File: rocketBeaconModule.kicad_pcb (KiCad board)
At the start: 2 copper layers, 57.2 x 57.2 mm, 96 parts, among them J1 TYPE-C-31-M-12, J2 PWR, J3 GND, J4 PWR, J5 GND, J6 Conn_01x03_Pin, P1 AntMount, U1 STM32F401CCU6, U2 CP2102N-Axx-xQFN20, U3 CC1200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

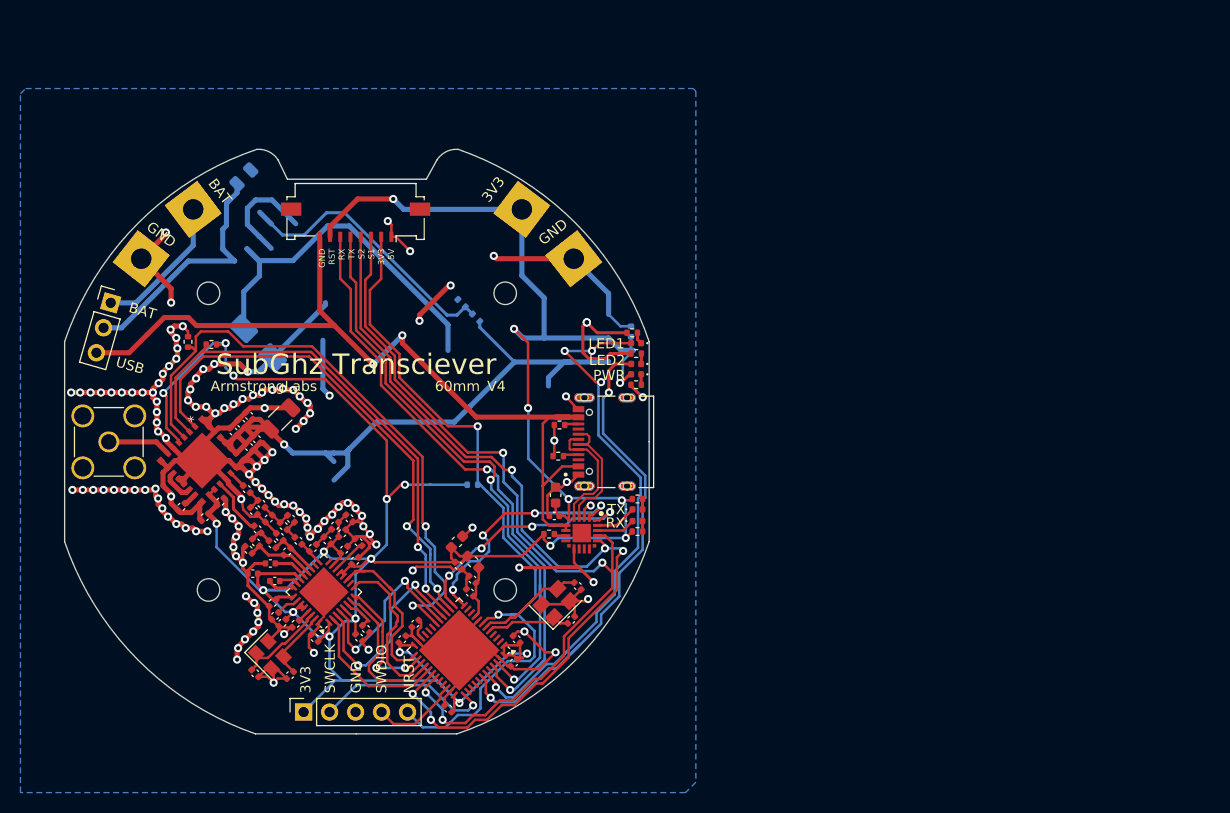
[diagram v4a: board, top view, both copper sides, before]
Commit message: added Mitsibushi Amp w/ supporting gate control circuitry, switching, and temperature monitoring
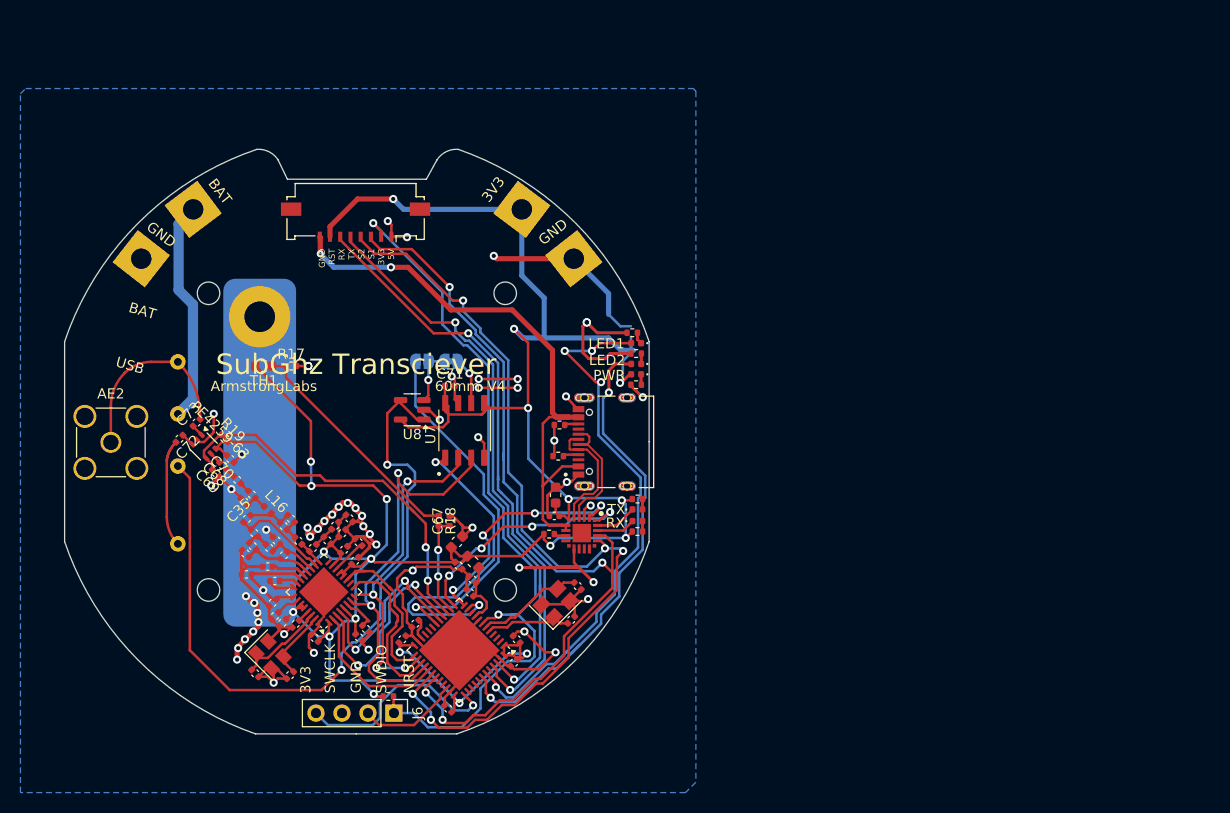
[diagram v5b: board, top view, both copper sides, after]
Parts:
- removed C14, C42: 10nF, Capacitor_SMD:C_0402_1005Metric
- removed C38, C39: 220pF, Capacitor_SMD:C_0402_1005Metric
- removed C40: 1uF, Capacitor_SMD:C_0402_1005Metric
- removed C41: 1nF, Capacitor_SMD:C_0402_1005Metric
- removed C43: 220uF, Capacitor_SMD:C_1206_3216Metric
- removed C44: 10uF, Capacitor_SMD:C_0402_1005Metric
- removed C45: 100uF, Capacitor_SMD:C_0805_2012Metric
- removed D6: SS34, Diode_SMD:D_SMA
- removed P1: AntMount, Connector_Coaxial:SMA_Amphenol_132134-11_Vertical
- removed R14, R15: 1k, Resistor_SMD:R_0402_1005Metric
- removed R16: 1.8k, Resistor_SMD:R_0402_1005Metric
- removed R2: 0, Capacitor_SMD:C_0402_1005Metric
- removed SWD1: FLASH, Connector_PinSocket_2.54mm:PinSocket_1x05_P2.54mm_Vertical
- removed U4: SKY65366-21, SKY65366:SKY65366-21_SKY
- added AE2: Antenna_Shield, Connector_Coaxial:SMA_Amphenol_132134-11_Vertical, F.Cu at (48.0, 126.8)
- added C67: 0.1uF, Capacitor_SMD:C_0402_1005Metric, F.Cu at (81.1, 134.5)
- added C68: 100pF, Capacitor_SMD:C_0402_1005Metric, F.Cu at (58.9, 129.1)
- added C69: 10nF, Capacitor_SMD:C_0402_1005Metric, F.Cu at (58.2, 129.8)
- added C70: 0.1uF, Capacitor_SMD:C_0402_1005Metric, F.Cu at (59.6, 128.4)
- added C71: 0.1uF, Capacitor_SMD:C_0402_1005Metric, F.Cu at (81.1, 121.3)
- added C72: 100pF, Capacitor_SMD:C_0402_1005Metric, F.Cu at (54.7, 126.4)
- added C73: 100pF, Capacitor_SMD:C_0402_1005Metric, F.Cu at (56.3, 124.9)
- added JP3: SolderJumper_2_Bridged, Jumper:SolderJumper-2_P1.3mm_Bridged_RoundedPad1.0x1.5mm, B.Cu at (81.2, 118.9)
- added JP4: SolderJumper_2_Open, Jumper:SolderJumper-2_P1.3mm_Open_RoundedPad1.0x1.5mm, B.Cu at (78.4, 118.9)
- added L16: 43nH, Inductor_SMD:L_0402_1005Metric, F.Cu at (63.3, 133.4)
- added PE4259-63: 4259-63, Package_TO_SOT_SMD:SOT-363_SC-70-6, F.Cu at (57.0, 127.2)
- added R19: 1k, Resistor_SMD:R_0402_1005Metric, F.Cu at (59.1, 126.4)
- added RFAMP2: RA07H4047M-101, RA07H4047m:RA07h4047M, B.Cu at (62.5, 127.8)
- added TH1: PT100, Resistor_SMD:R_0603_1608Metric, F.Cu at (62.9, 119.3)
- added U7: MCP41010, MCP41010:SOIC127P599X175-8N, F.Cu at (82.5, 125.6)
- added U8: MCP6001-OT, Package_TO_SOT_SMD:SOT-23-5, F.Cu at (77.4, 123.6)
- J6: value Conn_01x03_Pin -> Conn_01x04_Pin; footprint Connector_PinHeader_2.54mm:PinHeader_1x03_P2.54mm_Vertical -> Connector_PinHeader_2.54mm:PinHeader_1x04_P2.54mm_Vertical
- R1: moved to F.Cu
- R17: value 3.9k -> 100; moved to F.Cu
- R18: value 1k -> 1000; moved to F.Cu
- R9: value 18k -> 18
- moved J6 48.7 mm to (75.6, 153.3), turned to -90 degrees
- moved R18 26.4 mm to (80.0, 134.5), turned to -90 degrees
- moved R1 22.3 mm to (75.1, 151.6)
- moved R17 18.7 mm to (65.6, 119.3), turned to 0 degrees
- moved C35 2.13 mm to (61.3, 134.3), turned to 45 degrees
- moved C37 1.31 mm to (61.0, 132.6), turned to 135 degrees
- moved L7 1.31 mm to (61.7, 131.9)
- moved R13 1.31 mm to (60.3, 130.5)
- moved C24 0.63 mm to (61.2, 139.7)
- moved C32 0.48 mm to (61.1, 137.7)
- moved C33 0.48 mm to (63.4, 137.1)
- moved L2 0.48 mm to (64.9, 137.8)
- moved L4 0.48 mm to (64.2, 136.4)
- moved L6 0.48 mm to (62.0, 135.7)
- moved L3 0.48 mm to (61.8, 136.9)
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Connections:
- net SPI2_SCK renamed DPOT_SCLK
- net SPI_MOSI renamed DPOT_MOSI
- C1 pad 1: FEM_VPC -> +3.3V
- C12 pad 1: FEM_VPC -> +3.3V
- C13 pad 1: FEM_VPC -> +3.3V
- C15 pad 1: FEM_VPC -> +3.3V
- C17 pad 1: FEM_VPC -> +3.3V
- C18 pad 1: FEM_VPC -> +3.3V
- C19 pad 1: FEM_VPC -> +3.3V
- C2 pad 1: FEM_VPC -> +3.3V
- C22 pad 1: FEM_VPC -> +3.3V
- C24 pad 1: FEM_VPC -> +3.3V
- C26 pad 2: FEM_VPC -> +3.3V
- C27 pad 1: FEM_VPC -> +3.3V
- C28 pad 2: FEM_VPC -> +3.3V
- C29 pad 2: FEM_VPC -> +3.3V
- C35 pad 1: Net-(C34-Pad1) -> Net-(U3-TRX_SW)
- C35 pad 2: GND -> Net-(C34-Pad1)
- C4 pad 1: FEM_VPC -> +3.3V
- C5 pad 1: FEM_VPC -> +3.3V
- C7 pad 1: FEM_VPC -> +3.3V
- C8 pad 1: FEM_VPC -> +3.3V
- D1 pad 2: FEM_VPC -> +3.3V
- EX1 pad 7: FEM_VPC -> +3.3V
- FB1 pad 2: FEM_VPC -> +3.3V
- J2 pad 1: FEM_VPC -> +3.3V
- J6 pad 1: +BATT -> /NRST
- J6 pad 2: /HV_SUPPLY -> /SWDIO
- J6 pad 3: VBUS -> GND
- L6 pad 2: Net-(U4-RX0) -> Net-(U3-TRX_SW)
- L7 pad 1: Net-(C34-Pad1) -> Net-(C37-Pad1)
- L7 pad 2: Net-(C37-Pad1) -> Net-(L7-Pad2)
- R1 pad 2: FEM_VPC -> +3.3V
- R10 pad 1: FEM_VPC -> +3.3V
- R11 pad 1: FEM_VPC -> +3.3V
- R12 pad 1: FEM_VPC -> +3.3V
- R13 pad 1: Net-(C37-Pad1) -> Net-(L7-Pad2)
- R17 pad 1: Net-(U5-FB) -> Net-(R17-Pad1)
- R17 pad 2: +3V9 -> GND
- R18 pad 1: FEM_VPC -> Net-(R17-Pad1)
- R18 pad 2: GND -> TEMPSENSORADC
- R9 pad 2: FEM_VPC -> +3.3V
- U1 pad 1: FEM_VPC -> +3.3V
- U1 pad 11: unconnected-(U1-PA1-Pad11) -> DPOT_CS
- U1 pad 14: FEM_TR -> TEMPSENSORADC
- U1 pad 15: FEM_EN -> AMP_SW_CTRL
- U1 pad 18: FEM_BYP -> AMP_ON
- U1 pad 24: FEM_VPC -> +3.3V
- U1 pad 36: FEM_VPC -> +3.3V
- U1 pad 48: FEM_VPC -> +3.3V
- U2 pad 6: FEM_VPC -> +3.3V
- U3 pad 1: FEM_VPC -> +3.3V
- U3 pad 12: FEM_VPC -> +3.3V
- U3 pad 13: FEM_VPC -> +3.3V
- U3 pad 15: FEM_VPC -> +3.3V
- U3 pad 18: unconnected-(U3-TRX_SW-Pad18) -> Net-(U3-TRX_SW)
- U3 pad 22: FEM_VPC -> +3.3V
- U3 pad 25: FEM_VPC -> +3.3V
- U3 pad 27: FEM_VPC -> +3.3V
- U3 pad 28: FEM_VPC -> +3.3V
- U3 pad 5: FEM_VPC -> +3.3V
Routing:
- net FEM_VPC: track 301.6 -> 0.00 mm, vias 23 -> 0
- net +3.3V: track 0.00 -> 291.5 mm, vias 0 -> 21
- net GND: track 362.0 -> 210.1 mm, vias 128 -> 55
- net Net-(RFAMP2-GATE_VOLTAGE_(VGG)): track 0.00 -> 71.4 mm, vias 0 -> 2
- net +3V9: track 70.7 -> 0.00 mm, vias 1 -> 0
- net FEM_BYP: track 60.6 -> 0.00 mm, vias 2 -> 0
- net FEM_EN: track 52.1 -> 0.00 mm, vias 2 -> 0
- net FEM_TR: track 49.9 -> 0.00 mm, vias 2 -> 0
- net AMP_SW_CTRL: track 0.00 -> 38.4 mm, vias 0 -> 2
- net Net-(D6-K): track 37.0 -> 0.00 mm
- net AMP_ON: track 0.00 -> 35.5 mm, vias 0 -> 1
- net DPOT_CS: track 0.00 -> 33.0 mm, vias 0 -> 2
- net VBUS: track 84.0 -> 56.6 mm
- net Net-(U5-FB): track 27.4 -> 0.00 mm
- net DPOT_MOSI: track 15.3 -> 41.1 mm, vias 0 -> 2
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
